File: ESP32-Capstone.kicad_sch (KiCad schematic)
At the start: 23 parts, among them IC1 ESP32-C3FN4, IC2 W25Q32JVZPIQ, SW1 SW_SPST, Y1 40MHz

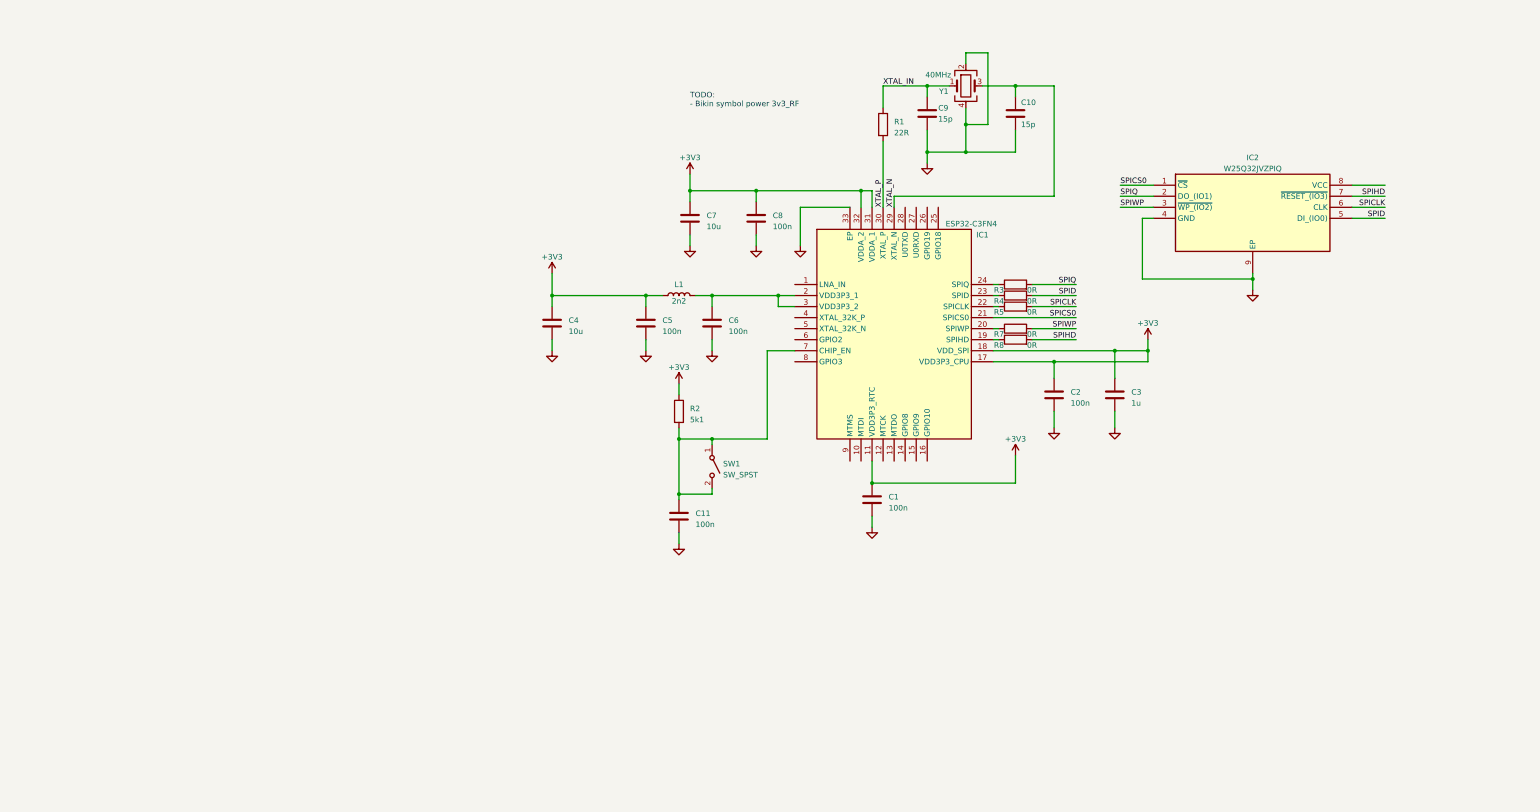
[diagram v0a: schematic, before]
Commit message: feat: add Power Supply, also UART and JTAG label
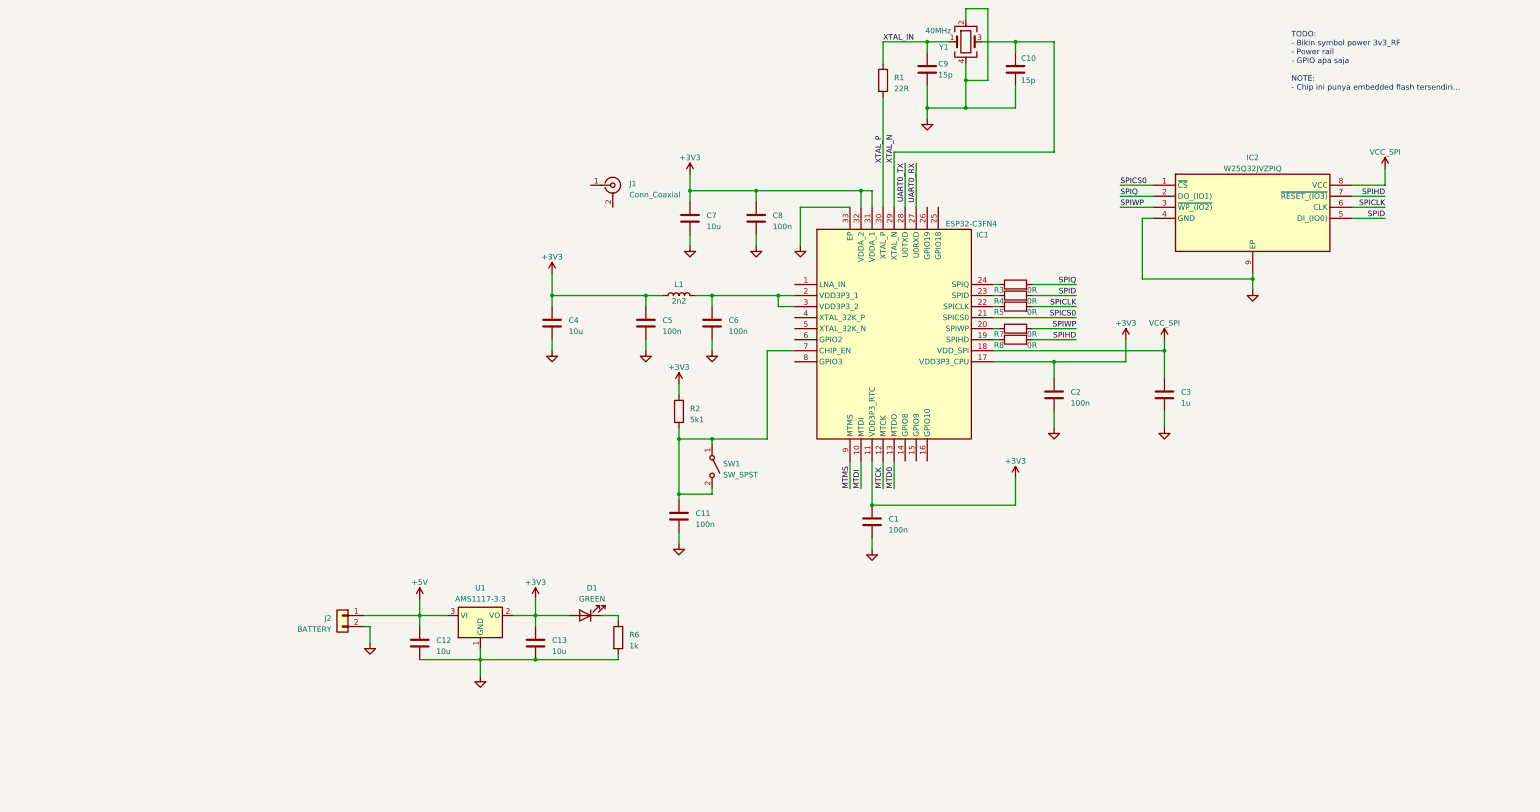
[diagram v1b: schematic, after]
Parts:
- added C12, C13: 10u, symbol Device:C
- added D1: GREEN, symbol Device:LED
- added J1: Conn_Coaxial, symbol Connector:Conn_Coaxial
- added J2: BATTERY, Connector_JST:JST_SUR_SM02B-SURS-TF_1x02-1MP_P0.80mm_Horizontal, symbol Connector_Generic:Conn_01x02
- added R6: 1k, symbol Device:R
- added U1: AMS1117-3.3, Package_TO_SOT_SMD:SOT-223-3_TabPin2, symbol Regulator_Linear:AMS1117-3.3
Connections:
- net +3V3: now also C13.1, D1.2 (A), U1.2 (VO); no longer C3.1, IC1.18 (VDD_SPI)
- net GND: now also C12.2, C13.2, J2.2 (Pin_2), R6.2, U1.1 (GND)
- net MTDI: now reaches IC1.10 (MTDI)
- net MTCK: now reaches IC1.12 (MTCK)
- net MTD0: now reaches IC1.13 (MTDO)
- net UART0_RX: now reaches IC1.27 (U0RXD)
- net UART0_TX: now reaches IC1.28 (U0TXD)
- net MTMS: now reaches IC1.9 (MTMS)
- net VCC_SPI: now reaches IC2.8 (VCC)
- net VCC_SPI: now also C3.1, IC1.18 (VDD_SPI)
- new net: D1.1 (K), R6.1
- new net +5V: C12.1, J2.1 (Pin_1), U1.3 (VI)
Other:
- note added: "TODO: - Bikin symbol power 3v3_RF - Power rail - GPIO apa saja NOTE: - Chip ini punya embedded flash tersendiri..."
- note removed: "TODO: - Bikin symbol power 3v3_RF"
- moved on the sheet: C1, C10, C3, C9, R1, Y1

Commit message: feat: add Antenna, JTAG, and UART. Schematic V1 is done.
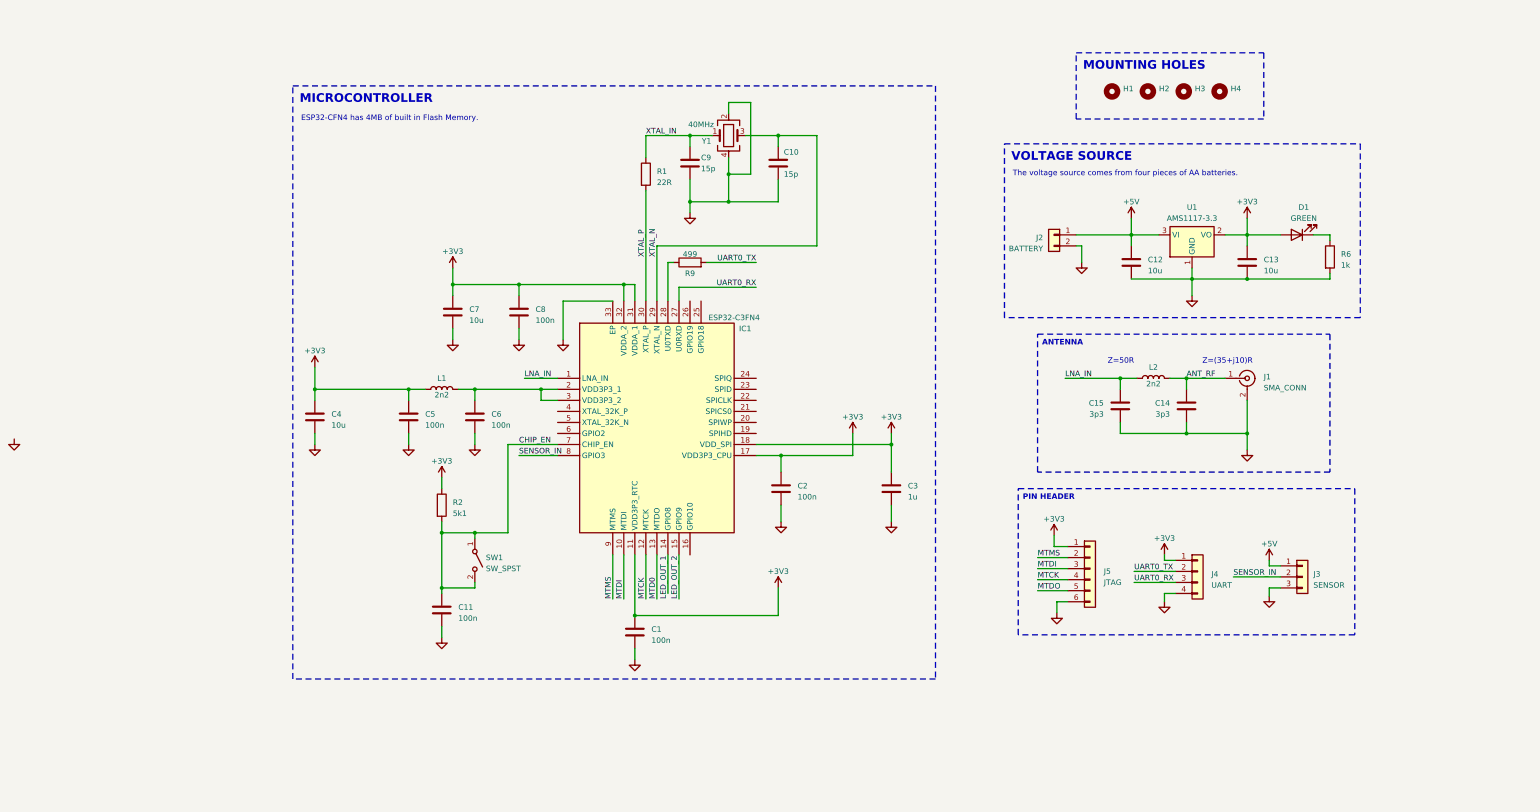
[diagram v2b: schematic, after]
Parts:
- removed IC2: W25Q32JVZPIQ, SON127P600X500X80-9N-D, symbol SamacSys_Parts:W25Q32JVZPIQ
- removed R3, R4, R5, R7, R8: 0R, symbol Device:R
- added C14, C15: 3p3, symbol Device:C
- added H1, H2, H3, H4: MountingHole, symbol Mechanical:MountingHole
- added J3: SENSOR, symbol Connector_Generic:Conn_01x03
- added J4: UART, symbol Connector_Generic:Conn_01x04
- added J5: JTAG, symbol Connector_Generic:Conn_01x06
- added L2: 2n2, symbol Device:L
- added R9: 499, symbol Device:R
- J1: value Conn_Coaxial -> SMA_CONN
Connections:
- net VCC_SPI is gone; now on net +3V3: C3.1, IC1.18 (VDD_SPI)
- net +3V3: now also J4.1 (Pin_1), J5.1 (Pin_1)
- net +5V: now also J3.1 (Pin_1)
- net GND: now also J1.2 (Ext), C14.2, C15.2, J3.3 (Pin_3), J4.4 (Pin_4), J5.6 (Pin_6)
- net MTCK: now also J5.4 (Pin_4)
- net MTDI: now also J5.3 (Pin_3)
- net MTMS: now also J5.2 (Pin_2)
- net UART0_RX: now also J4.3 (Pin_3)
- net UART0_TX: now also J4.2 (Pin_2), R9.2; no longer IC1.28 (U0TXD)
- net CHIP_EN: now reaches C11.1, IC1.7 (CHIP_EN), R2.2, SW1.1 (A), SW1.2 (B)
- net LNA_IN: now reaches IC1.1 (LNA_IN)
- net LNA_IN: now also C15.1, L2.2
- net LED_OUT_2: now reaches IC1.15 (GPIO9)
- net SENSOR_IN: now reaches IC1.8 (GPIO3)
- net SENSOR_IN: now also J3.2 (Pin_2)
- net ANT_RF: now reaches J1.1 (In)
- net ANT_RF: now also C14.1, L2.1
- net SPICS0: no longer names the net of IC1.21 (SPICS0)
- new net: IC1.28 (U0TXD), R9.1
- new net MTDO: J5.5 (Pin_5)
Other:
- note added: "ESP32-CFN4 has 4MB of built in Flash Memory."
- note added: "The voltage source comes from four pieces of AA batteries."
- note added: "Z=(35+j10)R"
- note added: "Z=50R"
- note removed: "TODO: - Bikin symbol power 3v3_RF - Power rail - GPIO apa saja NOTE: - Chip ini punya embedded flash tersendiri..."
- moved on the sheet: C1, C10, C11, C12, C13, C2, C3, C4, C5, C6, C7, C8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

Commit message: fix: update schematic picture
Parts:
- added D2: YELLOW, LED_SMD:LED_0603_1608Metric, symbol Device:LED
- added D3: BLUE, LED_SMD:LED_0603_1608Metric, symbol Device:LED
- added R3, R4: 1k, Resistor_SMD:R_0402_1005Metric, symbol Device:R
- C1, C10, C11, C12, C13, C14, C15, C2, C3, C4, C5, C6, C7, C8, C9: footprint (none) -> Capacitor_SMD:C_0402_1005Metric
- D1: footprint (none) -> LED_SMD:LED_0603_1608Metric
- H1, H2, H3, H4: footprint (none) -> MountingHole:MountingHole_2.2mm_M2_ISO14580
- IC1: footprint QFN50P500X500X90-33N-D -> SamacSys_Parts:QFN50P500X500X90-33N-D
- J1: footprint (none) -> Connector_Coaxial:SMA_Molex_73251-1153_EdgeMount_Horizontal
- J2: footprint Connector_JST:JST_SUR_SM02B-SURS-TF_1x02-1MP_P0.80mm_Horizontal -> Connector_JST:JST_EH_S2B-EH_1x02_P2.50mm_Horizontal
- J3: footprint (none) -> Connector_JST:JST_EH_S3B-EH_1x03_P2.50mm_Horizontal
- J4: footprint (none) -> Connector_PinHeader_2.54mm:PinHeader_1x04_P2.54mm_Vertical
- J5: footprint (none) -> Connector_PinHeader_2.54mm:PinHeader_1x06_P2.54mm_Vertical
- L1, L2: footprint (none) -> Inductor_SMD:L_0402_1005Metric
- R1, R2, R6, R9: footprint (none) -> Resistor_SMD:R_0402_1005Metric
- SW1: footprint (none) -> Button_Switch_SMD:SW_SPST_B3U-1000P
- Y1: footprint (none) -> Crystal:Crystal_SMD_SeikoEpson_FA238-4Pin_3.2x2.5mm
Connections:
- net MTD0 is gone; now on net MTDO: IC1.13 (MTDO)
- net GND: now also R3.2, R4.2
- net LED_OUT_1: now also IC1.14 (GPIO8), D2.2 (A)
- net LED_OUT_2: now also D3.2 (A)
- new net: D2.1 (K), R3.1
- new net: D3.1 (K), R4.1
- no-connect marks 0 -> 12
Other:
- note added: "Yellow LED indicates WiFi connection and Blue LED indicates MQTT connection."
- moved on the sheet: C2, C3, J3, J4, J5
